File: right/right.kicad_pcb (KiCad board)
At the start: 2 copper layers, 173.8 x 173.8 mm, 75 parts, among them J1 HDMI_C_1.4

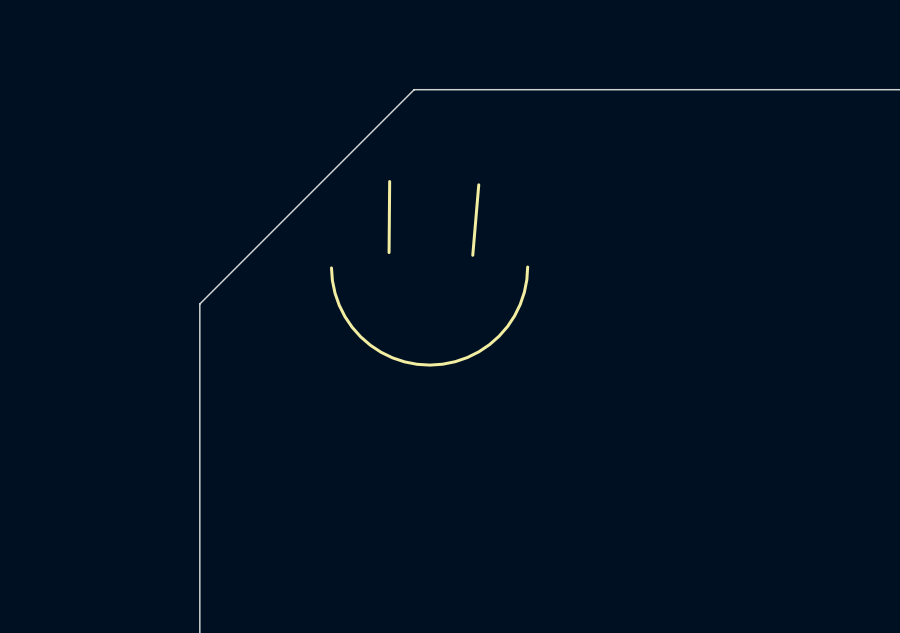
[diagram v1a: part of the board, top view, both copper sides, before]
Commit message: Add OSHW logo
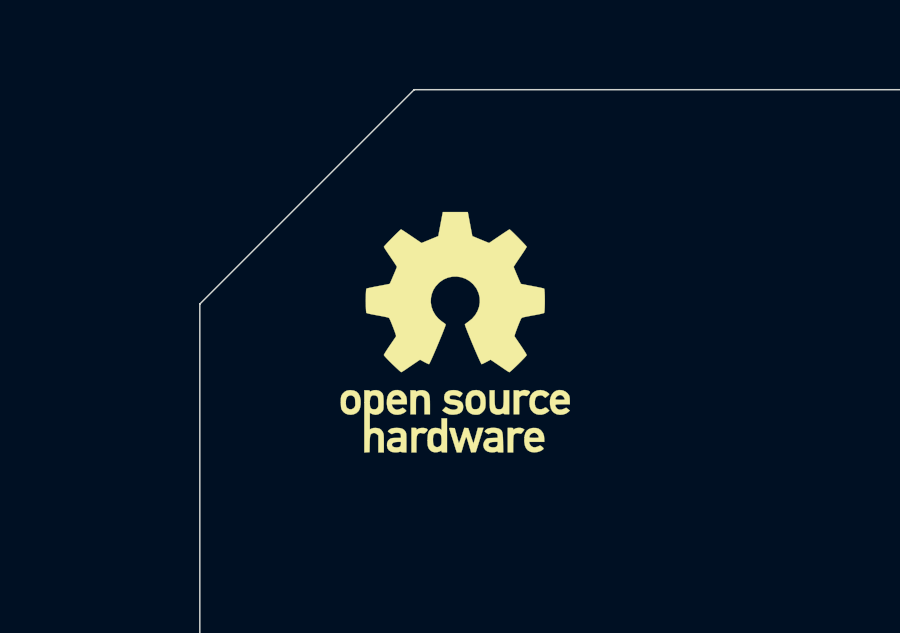
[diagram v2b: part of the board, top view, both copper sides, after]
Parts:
- removed the G*** at (107.2, 42.9)
- added REF**: OSHW-Logo_7.5x8mm_SilkScreen, Symbol:OSHW-Logo_7.5x8mm_SilkScreen, F.Cu at (108.5, 46.2)
